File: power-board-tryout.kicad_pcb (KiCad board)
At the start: 2 copper layers, 100 x 100 mm, 39 parts, among them J1 3V3_OUT, J2 Screw_Terminal_01x04, J3 5V_OUT, J4 AUX1_OUT, J5 AUX2_OUT, J6 AUX3_OUT, U1 MP1584-BREAKOUT-BOARD, U2 MP1584-BREAKOUT-BOARD, U3 MP1584-BREAKOUT-BOARD, U4 MP1584-BREAKOUT-BOARD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

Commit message: update,
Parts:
- removed JP8: Jumper_NO_Small, Jumper:SolderJumper-2_P1.3mm_Open_TrianglePad1.0x1.5mm
- removed JP9: Jumper_2_Open, Jumper:SolderJumper-2_P1.3mm_Open_TrianglePad1.0x1.5mm
- added C1: C104,0603, Capacitor_SMD:C_0603_1608Metric_Pad1.05x0.95mm_HandSolder, F.Cu at (80.8, 139.1)
- added C2: C106,0805, Capacitor_SMD:C_0805_2012Metric_Pad1.15x1.40mm_HandSolder, F.Cu at (82.6, 133.7)
- added C3: C151,0603, Capacitor_SMD:C_0603_1608Metric_Pad1.05x0.95mm_HandSolder, F.Cu at (87.0, 145.1)
- added C4: C106,0805, Capacitor_SMD:C_0805_2012Metric_Pad1.15x1.40mm_HandSolder, F.Cu at (73.8, 134.3)
- added C5: C106,0805, Capacitor_SMD:C_0805_2012Metric_Pad1.15x1.40mm_HandSolder, F.Cu at (73.8, 136.7)
- added J7: Conn_01x03_Female, Connector_PinHeader_2.54mm:PinHeader_1x02_P2.54mm_Vertical, F.Cu at (100.4, 136.2)
- added L1: L_15uH, w_smd_inductors:inductor_smd_6.8x3.8mm, F.Cu at (66.4, 140.3)
- added R11: R240,0603, Resistor_SMD:R_0603_1608Metric_Pad1.05x0.95mm_HandSolder, F.Cu at (83.8, 145.1)
- added R12: R104,0603, Resistor_SMD:R_0603_1608Metric_Pad1.05x0.95mm_HandSolder, F.Cu at (87.0, 133.9)
- added R13: R433,0603, Resistor_SMD:R_0603_1608Metric_Pad1.05x0.95mm_HandSolder, F.Cu at (88.6, 145.1)
- added R14: R104,0603, Resistor_SMD:R_0603_1608Metric_Pad1.05x0.95mm_HandSolder, F.Cu at (85.4, 145.1)
- D5: value LED_GREEN,0805 -> D_1N4148_T4; footprint LED_SMD:LED_0805_2012Metric_Pad1.15x1.40mm_HandSolder -> Diode_SMD:D_SOD-123
- J6: value AUX3_OUT -> Conn_01x03_Female; footprint footprint-lib:PinHeader_1x02_P2.54mm_power_output_terminal -> Connector_PinHeader_2.54mm:PinHeader_1x02_P2.54mm_Vertical
- R10: value R103,0805 -> R224,0603; footprint Resistor_SMD:R_0805_2012Metric_Pad1.15x1.40mm_HandSolder -> Resistor_SMD:R_0603_1608Metric_Pad1.05x0.95mm_HandSolder
- R9: value VAR_5V6,0805 -> R104,0603; footprint footprint-lib:VAR_0805 -> Resistor_SMD:R_0603_1608Metric_Pad1.05x0.95mm_HandSolder
- U5: value MP1584-BREAKOUT-BOARD -> MP1584; footprint footprint-lib:MP1584_buck_module -> footprint-lib:MP1584,SOIC-8_3.9x4.9mm_P1.27mm,thermal_via
- moved J6 52.6 mm to (57.4, 133.6)
- moved D5 27.4 mm to (77.8, 138.3), turned to 90 degrees
- moved R9 18.5 mm to (82.2, 145.1)
- moved R10 15.6 mm to (89.6, 142.3), turned to 180 degrees
- moved U5 9.82 mm to (84.8, 139.3), turned to 90 degrees
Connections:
- D5 pad 1: Net-(D5-Pad1) -> Net-(C1-Pad1)
- D5 pad 2: Net-(D5-Pad2) -> GND
- J6 pad 1: Net-(D5-Pad2) -> /PWR
- J6 pad 2: Net-(J6-Pad2) -> GND
- R10 pad 1: Net-(D5-Pad1) -> +5V
- R10 pad 2: Net-(J6-Pad2) -> Net-(R10-Pad2)
- R9 pad 1: Net-(D5-Pad2) -> /PWR
- R9 pad 2: Net-(J6-Pad2) -> Net-(R11-Pad1)
- U5 pad 1: /PWR -> Net-(C1-Pad1)
- U5 pad 2: GND -> Net-(R11-Pad1)
- U5 pad 3: Net-(J6-Pad2) -> Net-(C3-Pad1)
- U5 pad 4: Net-(JP9-Pad1) -> Net-(R10-Pad2)
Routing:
- net GND: track 137.1 -> 199.7 mm, vias 3 -> 5
- net +5V: track 0.00 -> 51.6 mm
- net Net-(J6-Pad2): track 44.7 -> 0.00 mm, vias 3 -> 0
- net /PWR: track 116.2 -> 142.9 mm, vias 0 -> 2
- net Net-(D5-Pad2): track 21.7 -> 0.00 mm, vias 3 -> 0
- net Net-(C1-Pad1): track 0.00 -> 20.3 mm
- net Net-(JP9-Pad1): track 19.4 -> 0.00 mm, vias 1 -> 0
- net Net-(R11-Pad1): track 0.00 -> 4.89 mm
- net Net-(D5-Pad1): track 4.40 -> 0.00 mm, vias 2 -> 0
- net Net-(R10-Pad2): track 0.00 -> 4.12 mm
- net Net-(R12-Pad1): track 0.00 -> 2.99 mm
- net Net-(C3-Pad1): track 0.00 -> 2.87 mm
- net Net-(C1-Pad2): track 0.00 -> 2.77 mm
- net Net-(C3-Pad2): track 0.00 -> 2.47 mm

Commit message: DRC ok,
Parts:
- J6: value Conn_01x03_Female -> POWER_IN
- J7: value Conn_01x03_Female -> POWER_OUT
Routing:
- net GND: track 199.7 -> 212.4 mm
- net Net-(D3-Pad2): track 24.4 -> 26.0 mm
- net Net-(D1-Pad2): vias 2 -> 3
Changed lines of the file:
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@@
     (thickness 1.6)
     (drawings 9)
-    (tracks 389)
+    (tracks 398)
     (zones 0)
     (modules 48)
@@
       (effects (font (size 1 1) (thickness 0.15)))
     )
-    (fp_text value Conn_01x03_Female (at 0 4.87) (layer F.Fab)
+    (fp_text value POWER_OUT (at 0 4.87) (layer F.Fab)
       (effects (font (size 1 1) (thickness 0.15)))
     )
@@
       (effects (font (size 1 1) (thickness 0.15)))
     )
-    (fp_text value Conn_01x03_Female (at 0 4.87) (layer F.Fab)
+    (fp_text value POWER_IN (at 0 4.87) (layer F.Fab)
       (effects (font (size 1 1) (thickness 0.15)))
     )
@@
     (descr MP1584)
     (tags "MP1584 SOIC-8")
+    (clearance 0.15)
     (attr smd)
     (fp_text reference U5 (at 0.254 -3.429 90) (layer F.SilkS)
@@
   (segment (start 110 55) (end 110 53) (width 0.8) (layer B.Cu) (net 1))
   (segment (start 110 53) (end 109.5 52.5) (width 0.8) (layer B.Cu) (net 1))
-  (segment (start 100 59.0625) (end 100 55.9) (width 0.8) (layer B.Cu) (net 1))
   (segment (start 99.1 55) (end 100 55.9) (width 0.8) (layer B.Cu) (net 1))
   (segment (start 99.1 55) (end 96.1 55) (width 0.8) (layer B.Cu) (net 1))
+  (segment (start 100 59.0625) (end 100 59.0625) (width 0.8) (layer B.Cu) (net 1))
+  (segment (start 100 59.0625) (end 100 55.9) (width 0.8) (layer B.Cu) (net 1))
+  (via (at 100 59.0625) (size 1) (drill 0.4) (layers F.Cu B.Cu) (net 1))
   (segment (start 106.025 58.975) (end 105.05 59.95) (width 0.8) (layer B.Cu) (net 2))
   (segment (start 106.025 55) (end 106.025 55) (width 0.8) (layer B.Cu) (net 2))
@@
   (segment (start 100.15 95.85) (end 100.15 95.75) (width 0.8) (layer B.Cu) (net 5))
   (segment (start 100.15 95.75) (end 99.4 95) (width 0.8) (layer B.Cu) (net 5))
-  (via (at 96.25 95) (size 1) (drill 0.4) (layers F.Cu B.Cu) (net 5))
-  (segment (start 99.4 95) (end 96.25 95) (width 0.8) (layer B.Cu) (net 5))
+  (via (at 95.85 95) (size 0.6) (drill 0.4) (layers F.Cu B.Cu) (net 5))
   (segment (start 103.975 95) (end 103.975 95) (width 0.8) (layer B.Cu) (net 5))
   (via (at 103.975 95) (size 1) (drill 0.4) (layers F.Cu B.Cu) (net 5))
+  (segment (start 99.4 95) (end 97.45 95) (width 0.8) (layer B.Cu) (net 5))
+  (segment (start 97.45 95) (end 95.85 95) (width 0.8) (layer B.Cu) (net 5))
+  (segment (start 97.45 95) (end 96.25 95) (width 0.8) (layer B.Cu) (net 5))
   (segment (start 106.025 95) (end 106.025 95) (width 0.8) (layer B.Cu) (net 6))
   (segment (start 106.025 97.95) (end 105 98.975) (width 0.8) (layer B.Cu) (net 6))
@@
   (segment (start 62.964 133.936) (end 65.729 133.936) (width 1) (layer F.Cu) (net 10))
   (segment (start 60.76 136.14) (end 62.964 133.936) (width 1) (layer F.Cu) (net 10))
+  (segment (start 83.275999 138.411) (end 86.323999 138.411) (width 1) (layer B.Cu) (net 10))
+  (segment (start 86.323999 138.411) (end 86.323999 140.189) (width 1) (layer B.Cu) (net 10))
+  (segment (start 86.323999 140.189) (end 83.275999 140.189) (width 1) (layer B.Cu) (net 10))
+  (segment (start 83.275999 140.189) (end 83.275999 138.411) (width 1) (layer B.Cu) (net 10))
+  (segment (start 83.275999 139.3) (end 86.323999 139.3) (width 1) (layer B.Cu) (net 10))
   (segment (start 65.729 106.604) (end 66.6792 106.604) (width 0.8) (layer B.Cu) (net 11))
   (segment (start 65.729 104.064) (end 66.6792 104.064) (width 0.8) (layer B.Cu) (net 11))
@@
   (segment (start 65.729 68.404) (end 65.729 66.604) (width 0.8) (layer B.Cu) (net 11))
   (segment (start 70 74.8) (end 70 77.993) (width 0.8) (layer B.Cu) (net 11))
+  (segment (start 84.165 134.24) (end 83.625 133.7) (width 0.4) (layer F.Cu) (net 11))
+  (segment (start 84.165 136.6) (end 84.165 134.24) (width 0.4) (layer F.Cu) (net 11))
+  (via (at 80.599999 142.9) (size 1) (drill 0.4) (layers F.Cu B.Cu) (net 11))
+  (segment (start 82.2 144.225) (end 81.924999 144.225) (width 0.4) (layer F.Cu) (net 11))
+  (segment (start 81.924999 144.225) (end 80.599999 142.9) (width 0.4) (layer F.Cu) (net 11))
+  (via (at 83.625 133.7) (size 1) (drill 0.4) (layers F.Cu B.Cu) (net 11))
+  (segment (start 80.599999 142.9) (end 80.6 136.725) (width 0.4) (layer B.Cu) (net 11))
+  (segment (start 80.6 136.725) (end 83.625 133.7) (width 0.4) (layer B.Cu) (net 11))
+  (segment (start 67.6 130.9) (end 65.729 129.029) (width 0.8) (layer B.Cu) (net 11))
+  (segment (start 74.3 130.9) (end 71.1 130.9) (width 0.8) (layer B.Cu) (net 11))
+  (segment (start 75.5 132.1) (end 74.3 130.9) (width 0.8) (layer B.Cu) (net 11))
+  (segment (start 71.1 130.9) (end 67.6 130.9) (width 0.8) (layer B.Cu) (net 11))
+  (segment (start 83.625 133.7) (end 82.025 132.1) (width 0.8) (layer B.Cu) (net 11))
+  (segment (start 82.025 132.1) (end 75.5 132.1) (width 0.8) (layer B.Cu) (net 11))
+  (segment (start 59.05 133.6) (end 57.4 133.6) (width 0.8) (layer F.Cu) (net 11))
+  (segment (start 60.533 133.6) (end 59.05 133.6) (width 0.8) (layer F.Cu) (net 11))
+  (segment (start 65.729 128.404) (end 60.533 133.6) (width 0.8) (layer F.Cu) (net 11))
+  (segment (start 65.729 126.604) (end 65.729 128.404) (width 0.8) (layer F.Cu) (net 11))
   (segment (start 84.271 75.936) (end 87.764 75.936) (width 0.8) (layer B.Cu) (net 12))
   (via (at 90 71.05) (size 1) (drill 0.4) (layers F.Cu B.Cu) (net 12))
@@
   (segment (start 91.2125 120.7375) (end 85.6125 120.7375) (width 0.8) (layer F.Cu) (net 18))
   (segment (start 85.6125 120.7375) (end 84.271 122.079) (width 0.8) (layer F.Cu) (net 18))
+  (segment (start 82.425 136.6) (end 80.8 138.225) (width 0.4) (layer F.Cu) (net 19))
+  (segment (start 82.894999 136.6) (end 82.425 136.6) (width 0.4) (layer F.Cu) (net 19))
   (segment (start 77.825 139.975001) (end 77.799999 139.95) (width 0.4) (layer F.Cu) (net 20))
   (segment (start 80.8 139.975) (end 77.825 139.975001) (width 0.4) (layer F.Cu) (net 20))
@@
   (segment (start 81.205 141.905) (end 82.1 141.905) (width 0.4) (layer F.Cu) (net 20))
   (segment (start 80.8 141.5) (end 81.205 141.905) (width 0.4) (layer F.Cu) (net 20))
-  (segment (start 84.165 134.24) (end 83.625 133.7) (width 0.4) (layer F.Cu) (net 11))
-  (segment (start 84.165 136.6) (end 84.165 134.24) (width 0.4) (layer F.Cu) (net 11))
-  (via (at 80.599999 142.9) (size 1) (drill 0.4) (layers F.Cu B.Cu) (net 11))
-  (segment (start 82.2 144.225) (end 81.924999 144.225) (width 0.4) (layer F.Cu) (net 11))
-  (segment (start 81.924999 144.225) (end 80.599999 142.9) (width 0.4) (layer F.Cu) (net 11))
-  (via (at 83.625 133.7) (size 1) (drill 0.4) (layers F.Cu B.Cu) (net 11))
-  (segment (start 80.599999 142.9) (end 80.6 136.725) (width 0.4) (layer B.Cu) (net 11))
-  (segment (start 80.6 136.725) (end 83.625 133.7) (width 0.4) (layer B.Cu) (net 11))
-  (segment (start 67.6 130.9) (end 65.729 129.029) (width 0.8) (layer B.Cu) (net 11))
-  (segment (start 74.3 130.9) (end 71.1 130.9) (width 0.8) (layer B.Cu) (net 11))
-  (segment (start 75.5 132.1) (end 74.3 130.9) (width 0.8) (layer B.Cu) (net 11))
-  (segment (start 71.1 130.9) (end 67.6 130.9) (width 0.8) (layer B.Cu) (net 11))
-  (segment (start 83.625 133.7) (end 82.025 132.1) (width 0.8) (layer B.Cu) (net 11))
-  (segment (start 82.025 132.1) (end 75.5 132.1) (width 0.8) (layer B.Cu) (net 11))
-  (segment (start 59.05 133.6) (end 57.4 133.6) (width 0.8) (layer F.Cu) (net 11))
-  (segment (start 60.533 133.6) (end 59.05 133.6) (width 0.8) (layer F.Cu) (net 11))
-  (segment (start 65.729 128.404) (end 60.533 133.6) (width 0.8) (layer F.Cu) (net 11))
-  (segment (start 65.729 126.604) (end 65.729 128.404) (width 0.8) (layer F.Cu) (net 11))
-  (segment (start 82.425 136.6) (end 80.8 138.225) (width 0.4) (layer F.Cu) (net 19))
-  (segment (start 82.894999 136.6) (end 82.425 136.6) (width 0.4) (layer F.Cu) (net 19))
   (segment (start 66.4 142.65) (end 76.65 142.65) (width 0.4) (layer F.Cu) (net 20))
   (segment (start 77.8 141.5) (end 77.8 139.95) (width 0.4) (layer F.Cu) (net 20))
@@
     (connect_pads (clearance 0.508))
     (min_thickness 0.254)
-    (fill (arc_segments 32) (thermal_gap 0.508) (thermal_bridge_width 0.508))
+    (fill yes (arc_segments 32) (thermal_gap 0.508) (thermal_bridge_width 0.508))
     (polygon
       (pts
@@
     (connect_pads (clearance 0.508))
     (min_thickness 0.254)
-    (fill (arc_segments 32) (thermal_gap 0.508) (thermal_bridge_width 0.508))
+    (fill yes (arc_segments 32) (thermal_gap 0.508) (thermal_bridge_width 0.508))
     (polygon
       (pts

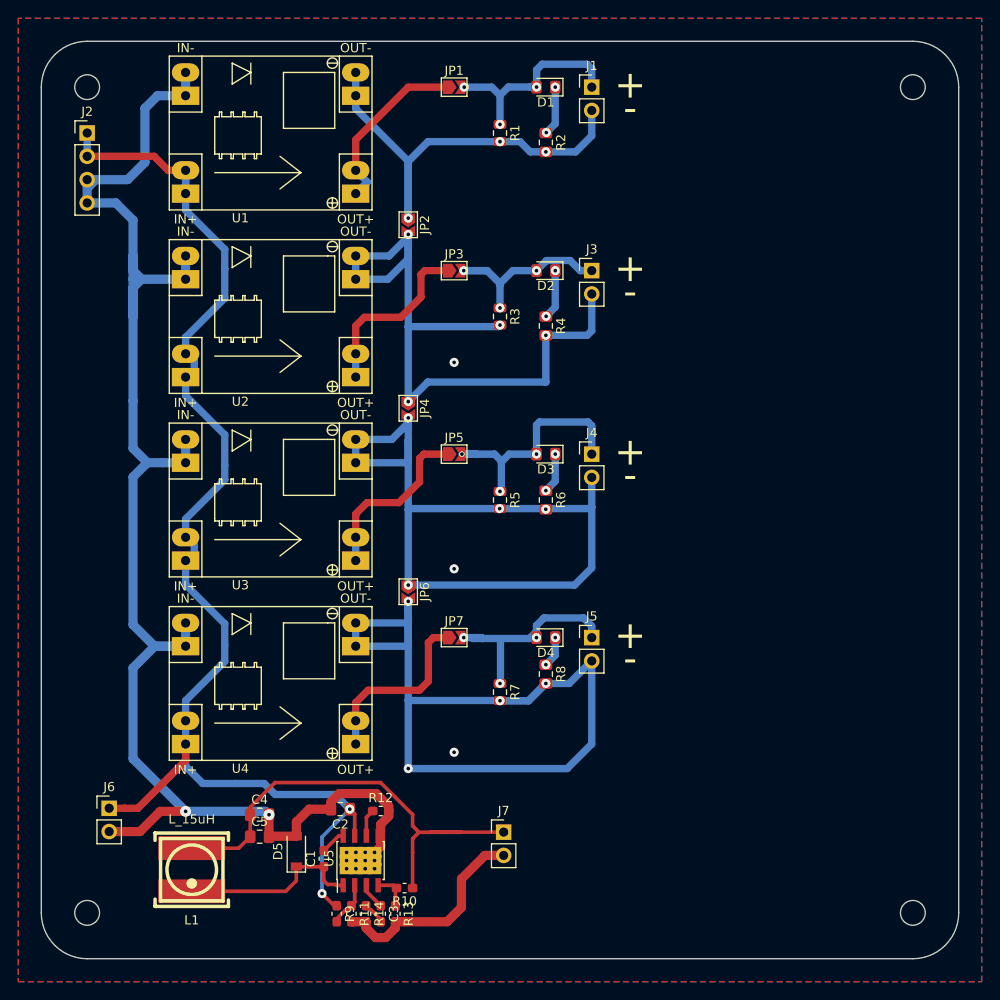
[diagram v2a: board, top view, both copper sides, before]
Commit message: update led on MP1584 and DRC ok,
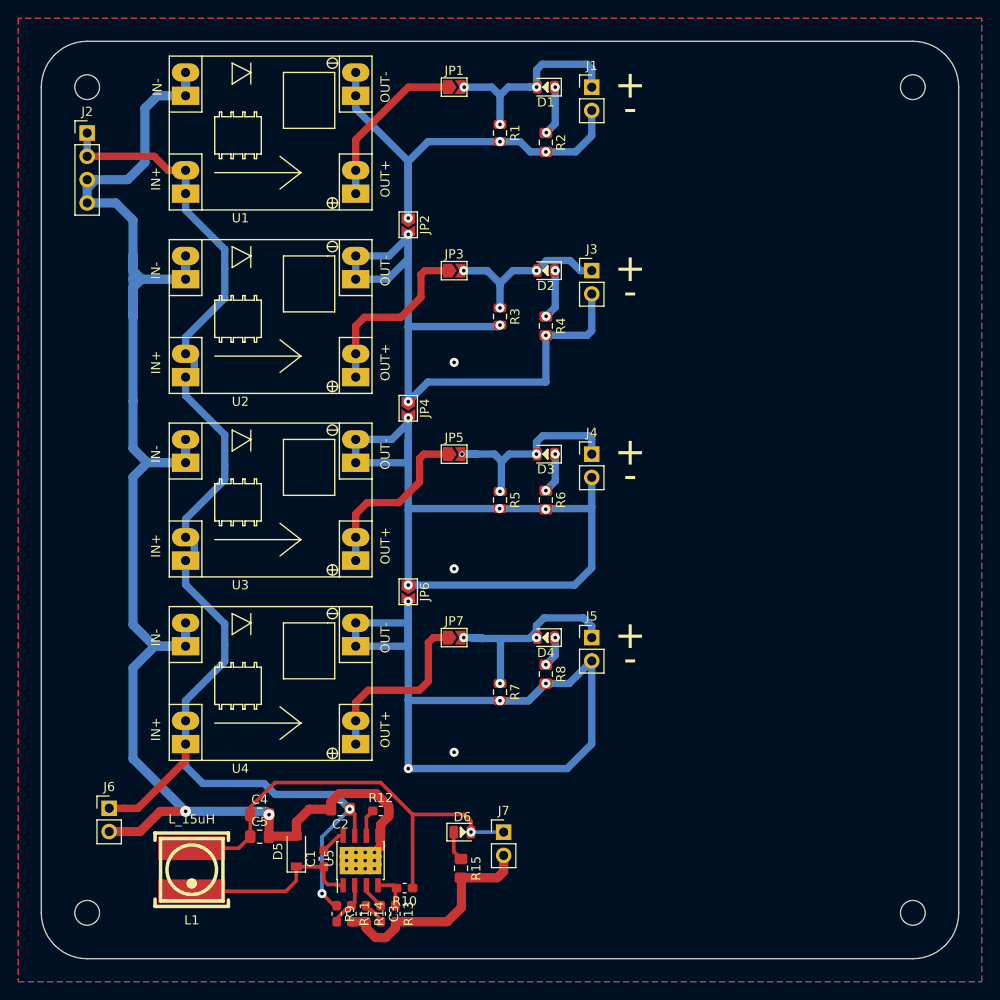
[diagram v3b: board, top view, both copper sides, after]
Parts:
- added D6: LED_GREEN,0805, footprint-lib:LED_0805_2012Metric, F.Cu at (95.9, 136.2)
- added R15: R103,0805, Resistor_SMD:R_0805_2012Metric_Pad1.15x1.40mm_HandSolder, F.Cu at (95.8, 140.2)
- D1, D2, D3, D4: footprint LED_SMD:LED_0805_2012Metric_Pad1.15x1.40mm_HandSolder -> footprint-lib:LED_0805_2012Metric
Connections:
- net +5V renamed Net-(C4-Pad1)
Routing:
- net Net-(D6-Pad1): track 0.00 -> 3.25 mm
- net Net-(D3-Pad2): track 26.0 -> 22.8 mm
- net Net-(C4-Pad1): track 51.6 -> 49.8 mm, vias 0 -> 1
- net Net-(JP1-Pad1): track 19.3 -> 18.3 mm
- net GND: track 212.4 -> 213.5 mm
